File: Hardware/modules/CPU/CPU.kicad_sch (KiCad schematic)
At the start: 16 parts, among them J1 ABORT, J2 SO/MX, J3 Bus_PCI_6502, J5 Bank Bridge A, J6 Bank Bridge B, J7 Bank Bridge C, U1 65C02 / 65816, U2 74LVC1GU04DRL, U3 74HC245, U4 74HC373

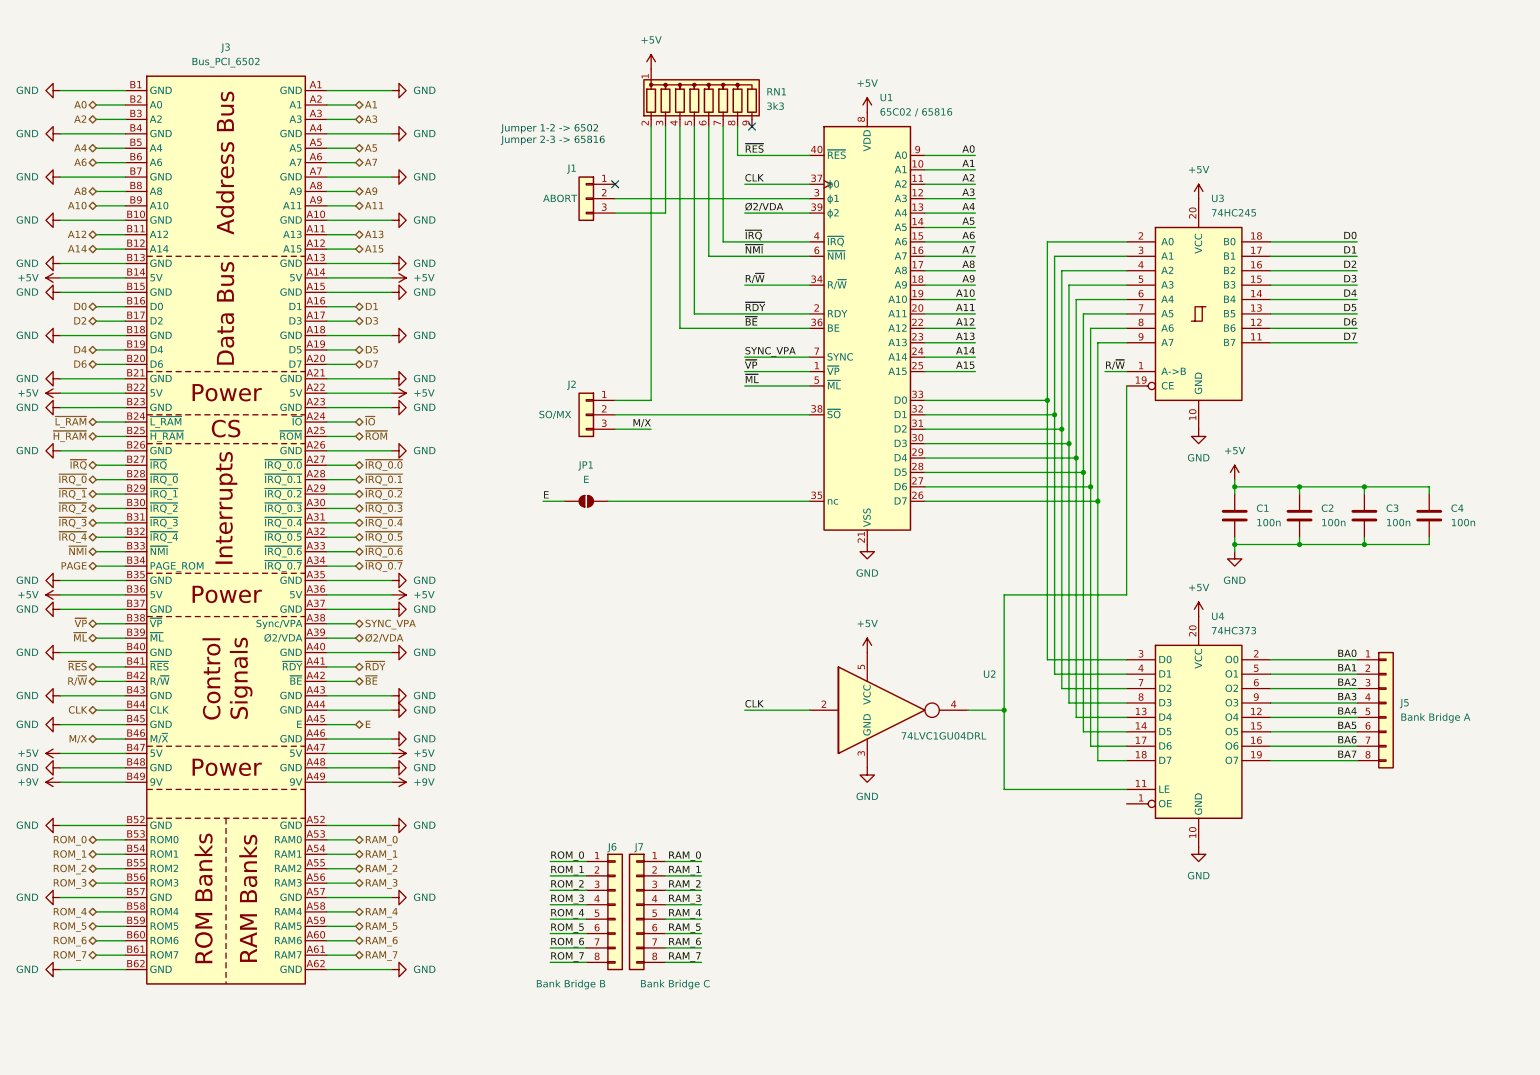
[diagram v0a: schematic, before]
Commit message: Hardware Update Add MyCPU VGA Module Beautify all Schematics minor Error corrections Readme Update
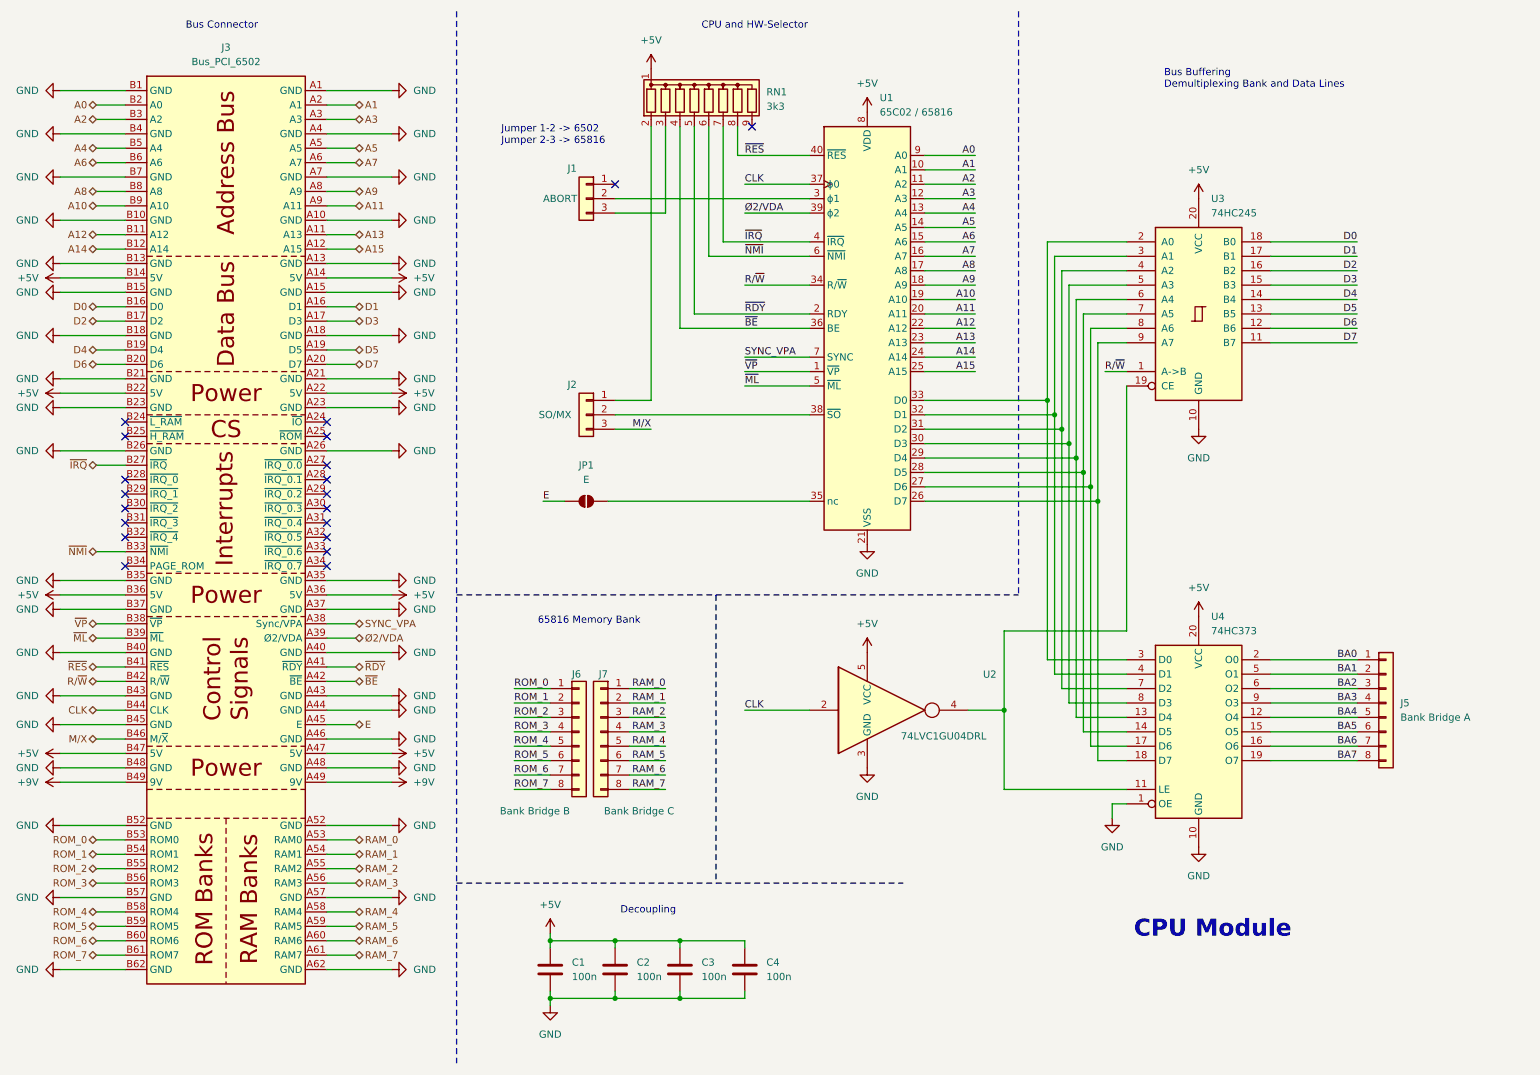
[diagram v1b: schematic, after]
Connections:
- net GND: now also U4.1 (OE)
- net PAGE: no longer names the net of J3.B34 (PAGE_ROM)
- net ~{H_RAM}: no longer names the net of J3.B25 (~{H_RAM})
- net ~{IO}: no longer names the net of J3.A24 (~{IO})
- net ~{IRQ_0.0}: no longer names the net of J3.A27 (~{IRQ_0.0})
- net ~{IRQ_0.1}: no longer names the net of J3.A28 (~{IRQ_0.1})
- net ~{IRQ_0.2}: no longer names the net of J3.A29 (~{IRQ_0.2})
- net ~{IRQ_0.3}: no longer names the net of J3.A30 (~{IRQ_0.3})
- net ~{IRQ_0.4}: no longer names the net of J3.A31 (~{IRQ_0.4})
- net ~{IRQ_0.5}: no longer names the net of J3.A32 (~{IRQ_0.5})
- net ~{IRQ_0.6}: no longer names the net of J3.A33 (~{IRQ_0.6})
- net ~{IRQ_0.7}: no longer names the net of J3.A34 (~{IRQ_0.7})
- net ~{IRQ_0}: no longer names the net of J3.B28 (~{IRQ_0})
- net ~{IRQ_1}: no longer names the net of J3.B29 (~{IRQ_1})
- net ~{IRQ_2}: no longer names the net of J3.B30 (~{IRQ_2})
- net ~{IRQ_3}: no longer names the net of J3.B31 (~{IRQ_3})
- net ~{IRQ_4}: no longer names the net of J3.B32 (~{IRQ_4})
- net ~{L_RAM}: no longer names the net of J3.B24 (~{L_RAM})
- net ~{ROM}: no longer names the net of J3.A25 (~{ROM})
- no-connect marks 2 -> 20
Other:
- note added: "65816 Memory Bank"
- note added: "Bus Buffering Demultiplexing Bank and Data Lines"
- note added: "Bus Connector"
- note added: "CPU Module"
- note added: "CPU and HW-Selector"
- note added: "Decoupling"
- company: (none) -> Synthron
- title: (none) -> S65xx Computer System
- moved on the sheet: C1, C2, C3, C4, J6, J7

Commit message: update CPU design to reference WDC design
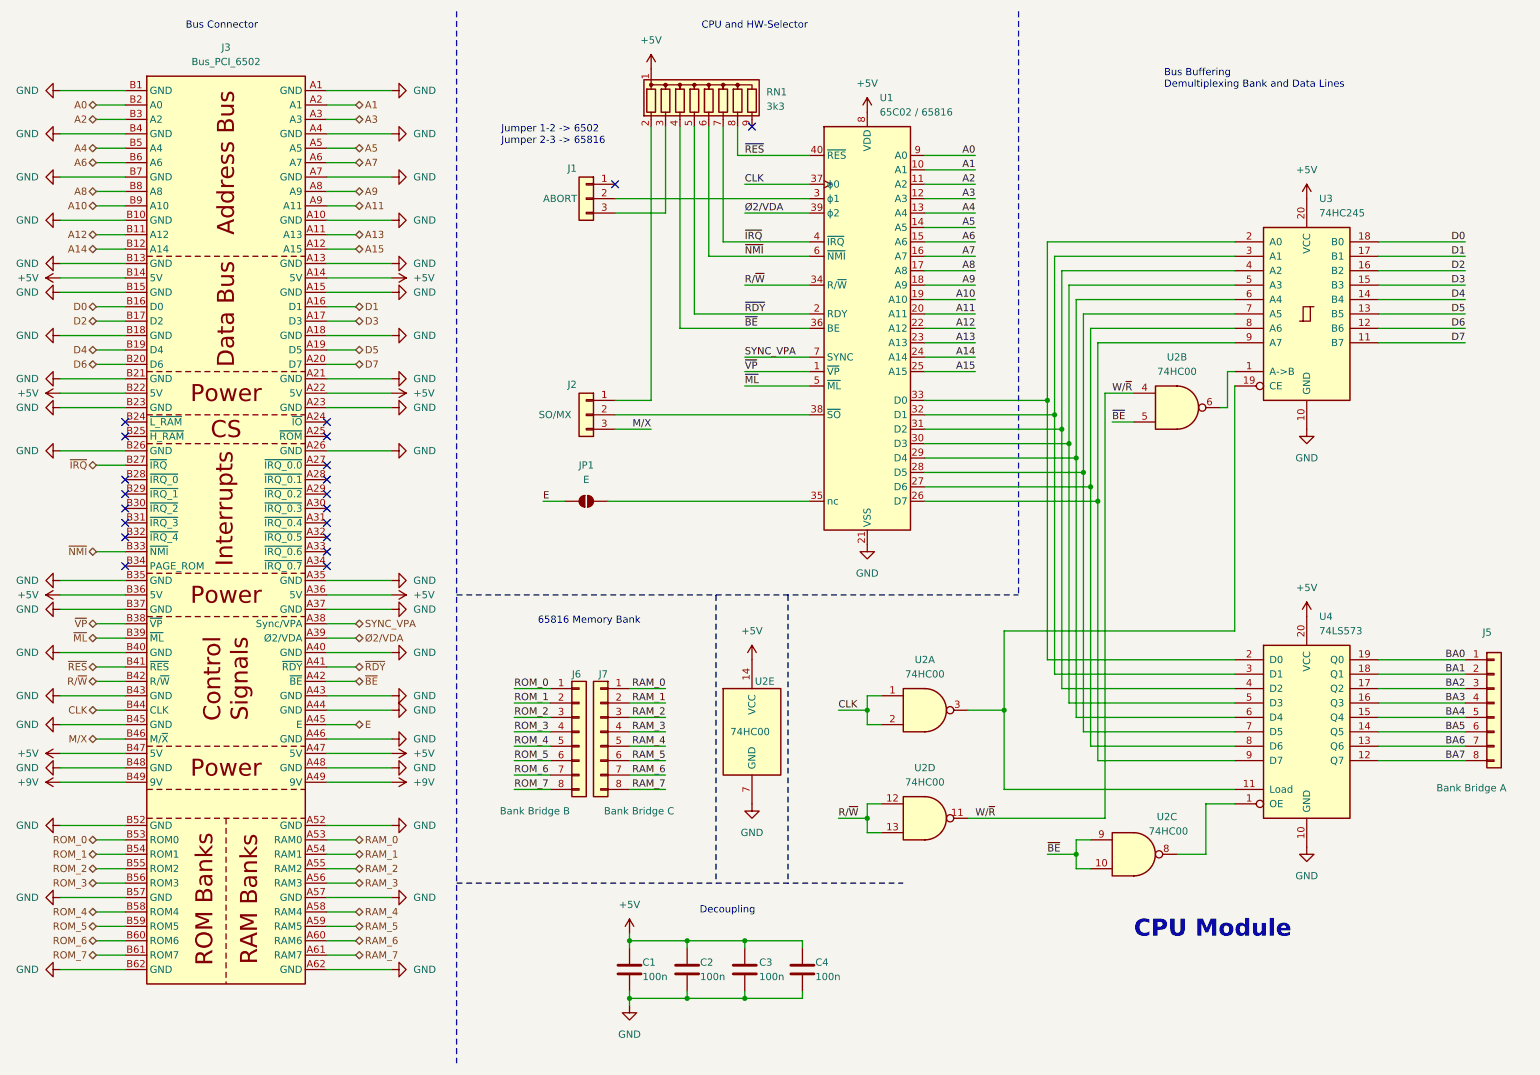
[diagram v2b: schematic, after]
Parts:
- removed U2: 74LVC1GU04DRL, Package_TO_SOT_SMD:SOT-553, symbol 74xGxx:74LVC1GU04DRL
- removed U4: 74HC373, Package_DIP:DIP-20_W7.62mm_LongPads, symbol 74xx:74HC373
- added U2: 74HC00, Package_DIP:DIP-14_W7.62mm, symbol 74xx:74HC00
- added U4: 74LS573, Package_DIP:DIP-20_W7.62mm, symbol 74xx:74LS573
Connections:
- net +5V: now also U2.14 (VCC), U4.20 (VCC)
- net BA0: now also U4.19 (Q0)
- net BA1: now also U4.18 (Q1)
- net BA2: now also U4.17 (Q2)
- net BA3: now also U4.16 (Q3)
- net BA4: now also U4.15 (Q4)
- net BA5: now also U4.14 (Q5)
- net BA6: now also U4.13 (Q6)
- net BA7: now also U4.12 (Q7)
- net CLK: now also U2.1, U2.2
- net GND: now also U2.7 (GND), U4.10 (GND)
- net R/~{W}: now also U2.12, U2.13; no longer U3.1 (A->B)
- net ~{BE}: now also U2.10, U2.5, U2.9
- net at U3.19 (CE): now also U2.3, U4.11 (Load)
- net at U1.33 (D0), U3.2 (A0): now also U4.2 (D0)
- net at U1.32 (D1), U3.3 (A1): now also U4.3 (D1)
- net at U1.31 (D2), U3.4 (A2): now also U4.4 (D2)
- net at U1.30 (D3), U3.5 (A3): now also U4.5 (D3)
- net at U1.29 (D4), U3.6 (A4): now also U4.6 (D4)
- net at U1.28 (D5), U3.7 (A5): now also U4.7 (D5)
- net at U1.27 (D6), U3.8 (A6): now also U4.8 (D6)
- net at U1.26 (D7), U3.9 (A7): now also U4.9 (D7)
- new net: U2.6, U3.1 (A->B)
- new net: U2.8, U4.1 (OE)
- new net W/~{R}: U2.11, U2.4
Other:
- moved on the sheet: C1, C2, C3, C4, J5, U3

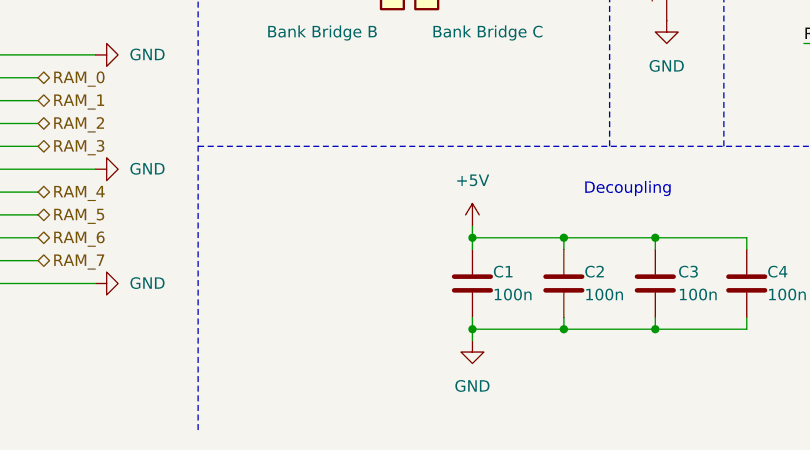
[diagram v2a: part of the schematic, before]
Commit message: Hardware Review Pt. 1 fix Address Decoding for Strobe Generators add bulk capacitance to every board fix wiring of Prototyping Board
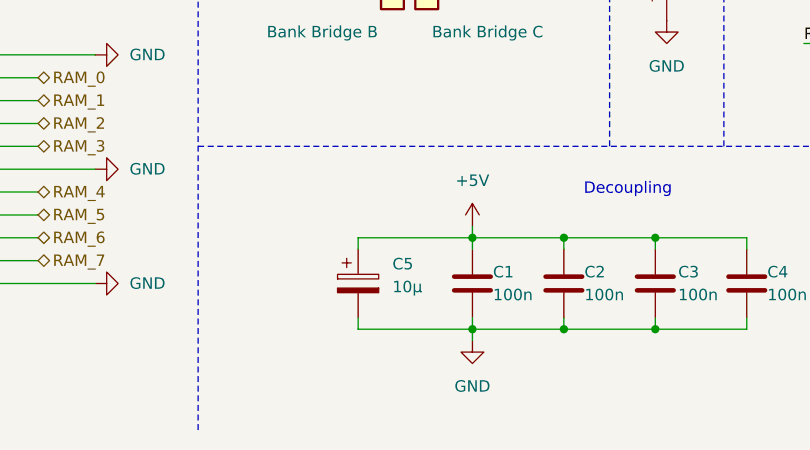
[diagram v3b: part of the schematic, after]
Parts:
- added C5: 10µ, Capacitor_THT:CP_Radial_D5.0mm_P2.50mm, symbol Device:C_Polarized
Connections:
- net +5V: now also C5.1
- net GND: now also C5.2
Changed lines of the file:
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@@
 	(wire
 		(pts
+			(xy 115.57 177.8) (xy 115.57 176.53)
+		)
+		(stroke
+			(width 0)
+			(type default)
+		)
+	)
+	(wire
+		(pts
 			(xy 260.35 127) (xy 275.59 127)
 		)
@@
 	(wire
 		(pts
+			(xy 115.57 176.53) (xy 128.27 176.53)
+		)
+		(stroke
+			(width 0)
+			(type default)
+		)
+	)
+	(wire
+		(pts
 			(xy 27.94 133.35) (xy 39.37 133.35)
 		)
@@
 	(wire
 		(pts
+			(xy 115.57 186.69) (xy 128.27 186.69)
+		)
+		(stroke
+			(width 0)
+			(type default)
+		)
+	)
+	(wire
+		(pts
 			(xy 144.78 53.34) (xy 144.78 33.02)
 		)
@@
 	(wire
 		(pts
+			(xy 115.57 185.42) (xy 115.57 186.69)
+		)
+		(stroke
+			(width 0)
+			(type default)
+		)
+	)
+	(wire
+		(pts
 			(xy 189.23 63.5) (xy 180.34 63.5)
 		)
@@
 					(unit 1)
 				)
+			)
+		)
+	)
+	(symbol
+		(lib_id "Device:C_Polarized")
+		(at 115.57 181.61 0)
+		(unit 1)
+		(exclude_from_sim no)
+		(in_bom yes)
+		(on_board yes)
+		(dnp no)
+		(fields_autoplaced yes)
+		(property "Reference" "C5"
+			(at 119.38 179.4509 0)
+			(effects
+				(font
+					(size 1.27 1.27)
+				)
+				(justify left)
+			)
+		)
+		(property "Value" "10µ"
+			(at 119.38 181.9909 0)
+			(effects
+				(font
+					(size 1.27 1.27)
+				)
+				(justify left)
+			)
+		)
+		(property "Footprint" "Capacitor_THT:CP_Radial_D5.0mm_P2.50mm"
+			(at 116.5352 185.42 0)
+			(effects
+				(font
+					(size 1.27 1.27)
+				)
+				(hide yes)
+			)
+		)
+		(property "Datasheet" "~"
+			(at 115.57 181.61 0)
+			(effects
+				(font
+					(size 1.27 1.27)
+				)
+				(hide yes)
+			)
+		)
+		(property "Description" "Polarized capacitor"
+			(at 115.57 181.61 0)
+			(effects
+				(font
+					(size 1.27 1.27)
+				)
+				(hide yes)
+			)
+		)
+		(pin "1"
+		)
+		(pin "2"
+		)
+		(instances
+			(project ""
+				(path "/941ebc74-12ab-4d35-9deb-0dbc73ea5676"
+					(reference "C5")
+					(unit 1)
+				)
